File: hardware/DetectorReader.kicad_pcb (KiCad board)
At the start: 2 copper layers, 51.8 x 27.5 mm, 60 parts, among them J1 10118194-0001LF, J2 Combo_Conn, J3 SMA_Conn, J4 SMA_Conn, J5 SMA_Conn, J6 Conn_Signal, J7 Conn_Amp1, J8 Conn_Amp2, J9 Conn_TriggerOut, Q1 BC847C,215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

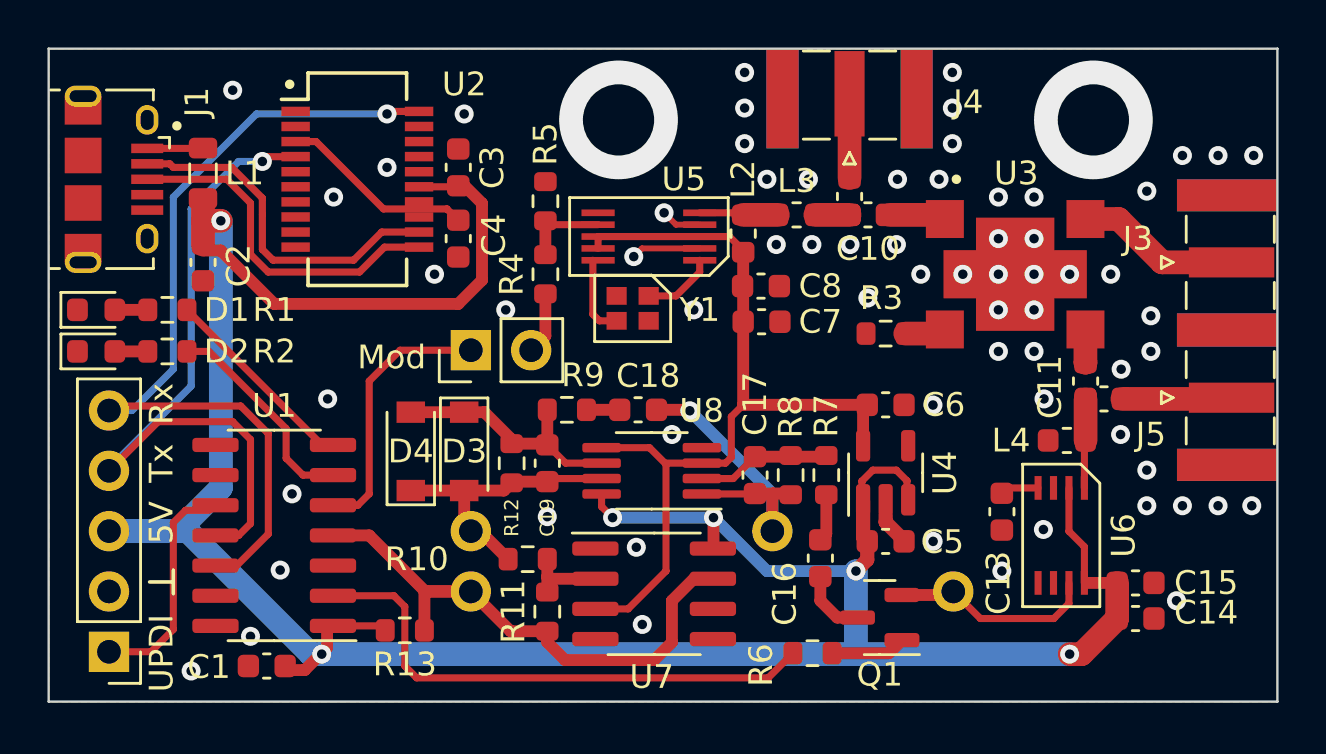
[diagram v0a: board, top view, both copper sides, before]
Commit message: added PA and changed directional coupler
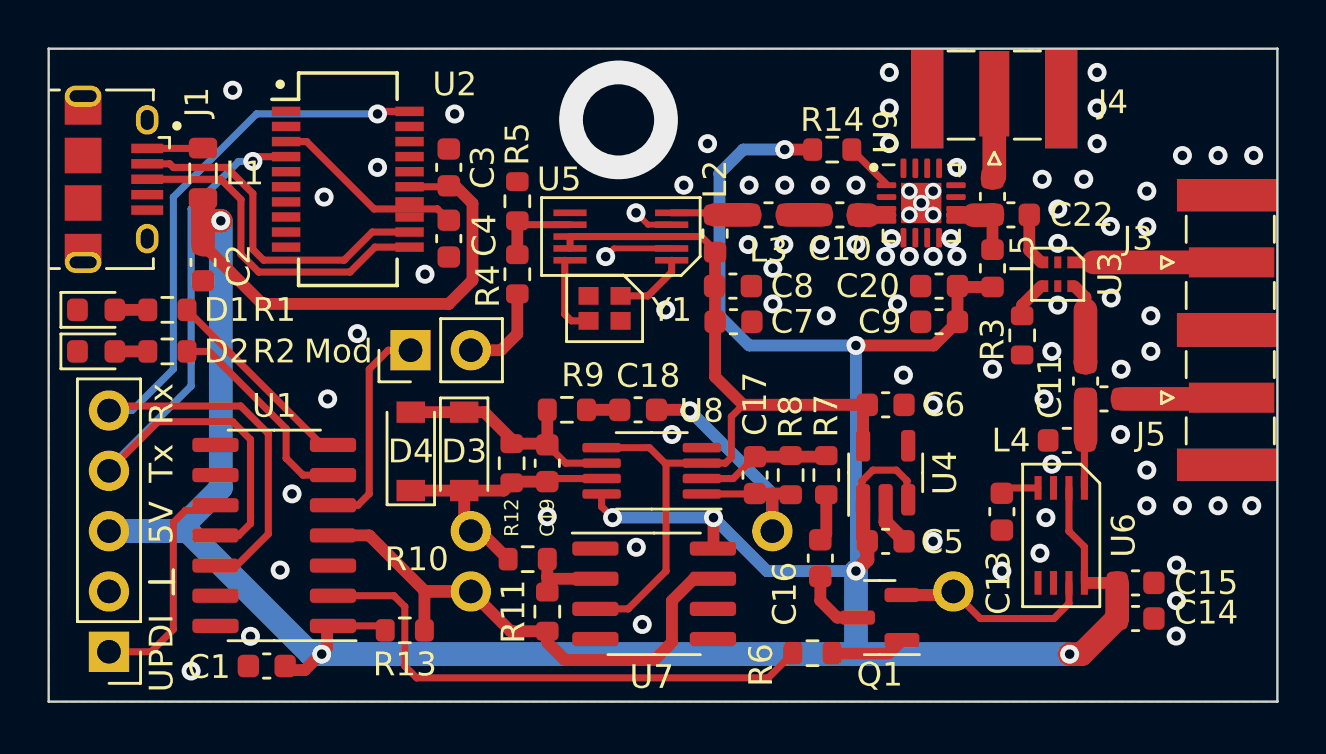
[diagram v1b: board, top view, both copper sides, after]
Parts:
- added C20: 100p, Capacitor_SMD:C_0603_1608Metric, F.Cu at (147.5, 82.0)
- added C21: 100p, Capacitor_SMD:C_0603_1608Metric, F.Cu at (149.8, 78.2)
- added C22: 100p, Capacitor_SMD:C_0603_1608Metric, F.Cu at (150.5, 79.0)
- added L5: 22n, Inductor_SMD:L_0603_1608Metric, F.Cu at (149.8, 81.2)
- added R14: 1.5k, Resistor_SMD:R_0603_1608Metric, F.Cu at (143.0, 76.2)
- added U9: GRF5040, Package_DFN_QFN:QFN-16-1EP_3x3mm_P0.5mm_EP1.7x1.7mm, F.Cu at (146.8, 78.5)
- C9: value 1.5p -> 100n
- U3: value XC0900P-10S -> HHM22137A2; footprint ProjLib:Xinger2 -> ProjLib:EIA0603
- moved C9 6.48 mm to (147.5, 83.5), turned to 180 degrees
- moved J4 6.09 mm to (149.8, 74.1)
- moved R3 5.75 mm to (151.0, 84.1), turned to -90 degrees
- moved SW1 2.54 mm to (125.2, 84.7)
- moved U3 1.79 mm to (152.5, 81.5), turned to 180 degrees
- moved C10 1.18 mm to (143.3, 79.0)
- moved C7 1.18 mm to (138.8, 83.5)
- moved C8 1.18 mm to (138.8, 82.0)
- moved L2 1.18 mm to (138.1, 79.8)
- moved L3 1.18 mm to (140.3, 79.0)
- moved U5 1.18 mm to (134.1, 79.9)
- moved Y1 1.18 mm to (133.4, 82.9)
- moved R4 1.18 mm to (129.7, 81.5)
- moved R5 1.18 mm to (129.7, 78.4)
- moved C3 0.40 mm to (126.8, 77.0)
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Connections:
- C10 pad 1: /RF_Tx/RfOut -> /RF_Tx/ModMatched
- C10 pad 2: /RF_Tx/ModOutSelect -> Net-(C10-Pad2)
- C9 pad 1: /RF_Tx/ModOutSelect -> +5V
- C9 pad 2: Net-(C9-Pad2) -> GND
- J4 pad 1: Net-(C9-Pad2) -> Net-(J4-Pad1)
- L3 pad 2: /RF_Tx/ModOutSelect -> Net-(C10-Pad2)
- U3 pad 1: /RF_Tx/RfOut -> Net-(J3-Pad1)
- U3 pad 2: Net-(J3-Pad1) -> GND
- U3 pad 3: /RF_Rx/DetectorIn -> /RF_Tx/RfOut
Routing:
- net +5V: track 119.8 -> 153.2 mm, vias 6 -> 8
- net Net-(J4-Pad1): track 0.00 -> 3.73 mm
- net Net-(C9-Pad2): track 3.70 -> 0.00 mm
- net /RF_Tx/PAOutSelect: track 0.00 -> 3.18 mm
- net /ReaderPulses: track 11.3 -> 9.05 mm
- net Net-(R14-Pad2): track 0.00 -> 2.11 mm
- net /RF_Rx/DetectorIn: track 1.40 -> 3.42 mm
- net Net-(C10-Pad2): track 0.00 -> 1.44 mm
- net /RF_Tx/ModOutSelect: track 1.44 -> 0.00 mm
- net /RF_Tx/ModMatched: track 0.00 -> 1.37 mm
- net /RF_Tx/Mod: track 2.62 -> 3.93 mm
- net GND: vias 68 -> 85
